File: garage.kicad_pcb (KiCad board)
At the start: 2 copper layers, 90 x 100 mm, 32 parts, among them J1 AC L/N, J2 Gate, K1 Relay_SPST-NO, K2 Relay_SPST-NO, Q1 2N5551, Q2 2N5551, SW1 Button, SW2 Radio, U1 LM2940T-5.0/NOPB, U2 ACS712xLCTR-05B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

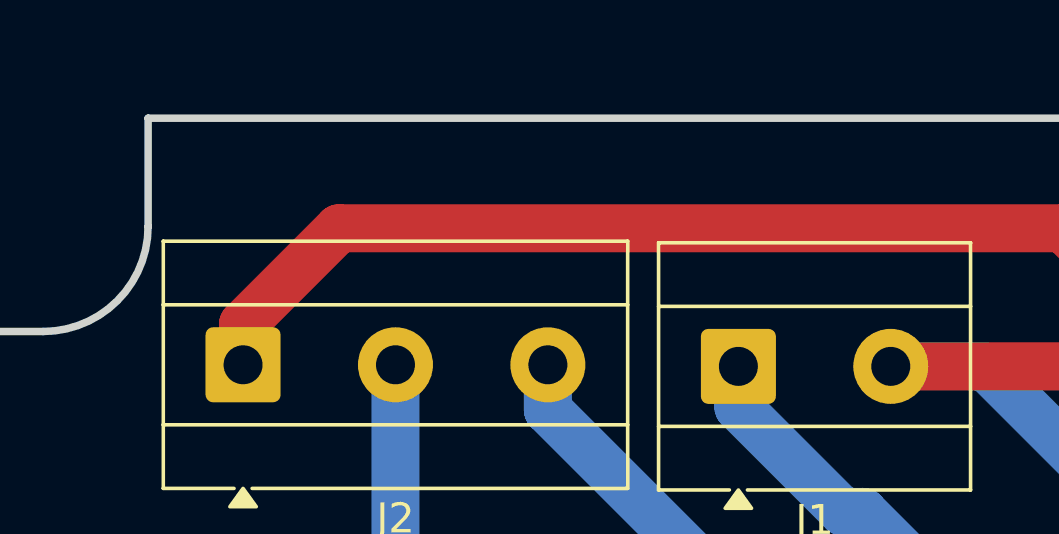
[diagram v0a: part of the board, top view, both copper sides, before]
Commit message: Reorganize and make suitable for publication.
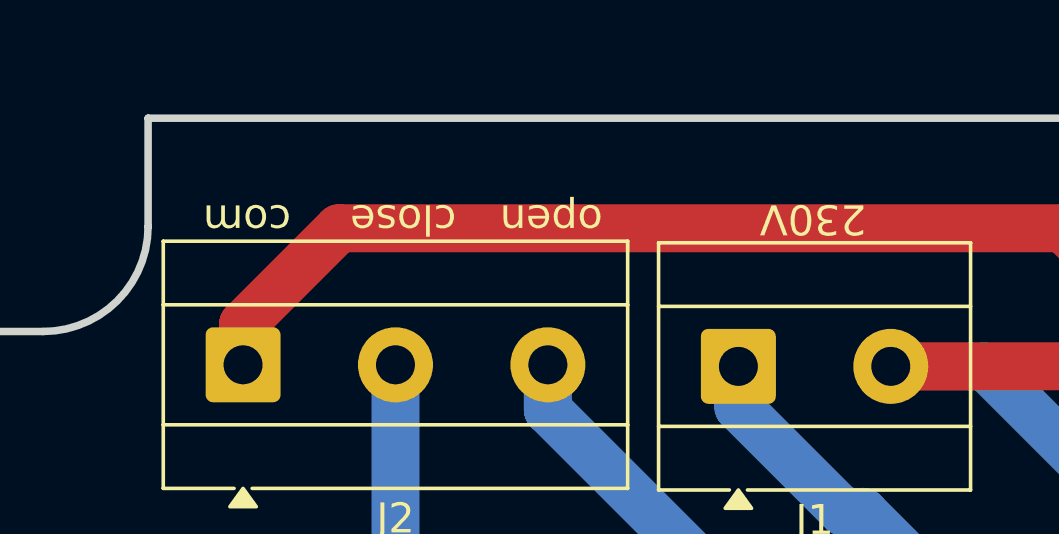
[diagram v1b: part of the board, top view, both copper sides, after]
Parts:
- RV1: value R_Potentiometer -> 10k
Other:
- board text added: "https://github.com/macdems/Garage"
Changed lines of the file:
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@@
 		(property ki_fp_filters "R_*")
 		(sheetname "/")
-		(sheetfile "Garaż.kicad_sch")
+		(sheetfile "garage.kicad_sch")
 		(attr through_hole)
 		(fp_line
@@
 		(property ki_fp_filters "SOIC*3.9x4.9mm*P1.27mm* DIP*W7.62mm* TO*99* OnSemi*Micro8* TSSOP*3x3mm*P0.65mm* TSSOP*4.4x3mm*P0.65mm* MSOP*3x3mm*P0.65mm* SSOP*3.9x4.9mm*P0.635mm* LFCSP*2x2mm*P0.5mm* *SIP* SOIC*5.3x6.2mm*P1.27mm*")
 		(sheetname "/")
-		(sheetfile "Garaż.kicad_sch")
+		(sheetfile "garage.kicad_sch")
 		(attr through_hole)
 		(fp_line
@@
 		(property ki_fp_filters "Connector*:*_1x??_*")
 		(sheetname "/")
-		(sheetfile "Garaż.kicad_sch")
+		(sheetfile "garage.kicad_sch")
 		(attr through_hole)
 		(fp_line
@@
 			(layer "F.Fab")
 		)
+		(fp_text user "close"
+			(at 7.106191 -5.4356 180)
+			(unlocked yes)
+			(layer "F.SilkS")
+			(effects
+				(font
+					(size 1 1)
+					(thickness 0.1)
+				)
+				(justify left bottom)
+			)
+		)
+		(fp_text user "open"
+			(at 11.9888 -5.4356 180)
+			(unlocked yes)
+			(layer "F.SilkS")
+			(effects
+				(font
+					(size 1 1)
+					(thickness 0.1)
+				)
+				(justify left bottom)
+			)
+		)
+		(fp_text user "com"
+			(at 1.597619 -5.4356 180)
+			(unlocked yes)
+			(layer "F.SilkS")
+			(effects
+				(font
+					(size 1 1)
+					(thickness 0.1)
+				)
+				(justify left bottom)
+			)
+		)
 		(fp_text user "${REFERENCE}"
 			(at 5.08 3 0)
@@
 		(property ki_fp_filters "R_*")
 		(sheetname "/")
-		(sheetfile "Garaż.kicad_sch")
+		(sheetfile "garage.kicad_sch")
 		(attr through_hole)
 		(fp_line
@@
 		(property ki_fp_filters "MountingHole*")
 		(sheetname "/")
-		(sheetfile "Garaż.kicad_sch")
+		(sheetfile "garage.kicad_sch")
 		(attr exclude_from_pos_files exclude_from_bom)
 		(fp_circle
@@
 		(property ki_fp_filters "CP_*")
 		(sheetname "/")
-		(sheetfile "Garaż.kicad_sch")
+		(sheetfile "garage.kicad_sch")
 		(attr through_hole)
 		(fp_line
@@
 		(property ki_fp_filters "C_*")
 		(sheetname "/")
-		(sheetfile "Garaż.kicad_sch")
+		(sheetfile "garage.kicad_sch")
 		(attr through_hole)
 		(fp_line
@@
 		)
 		(sheetname "/")
-		(sheetfile "Garaż.kicad_sch")
+		(sheetfile "garage.kicad_sch")
 		(attr through_hole)
 		(fp_line
@@
 		(property ki_fp_filters "NDE3")
 		(sheetname "/")
-		(sheetfile "Garaż.kicad_sch")
+		(sheetfile "garage.kicad_sch")
 		(attr through_hole)
 		(fp_line
@@
 		(property ki_fp_filters "SOIC*3.9x4.9m*P1.27mm*")
 		(sheetname "/")
-		(sheetfile "Garaż.kicad_sch")
+		(sheetfile "garage.kicad_sch")
 		(attr smd)
 		(fp_line
@@
 		(property ki_fp_filters "Connector*:*_1x??_*")
 		(sheetname "/")
-		(sheetfile "Garaż.kicad_sch")
+		(sheetfile "garage.kicad_sch")
 		(attr through_hole)
 		(fp_line
@@
 			(layer "F.Fab")
 		)
+		(fp_text user "230V"
+			(at 2.4892 -5.4881 180)
+			(unlocked yes)
+			(layer "F.SilkS")
+			(effects
+				(font
+					(size 1 1)
+					(thickness 0.1)
+				)
+				(justify bottom)
+			)
+		)
 		(fp_text user "${REFERENCE}"
 			(at 2.54 3 0)
@@
 		(property ki_fp_filters "R_*")
 		(sheetname "/")
-		(sheetfile "Garaż.kicad_sch")
+		(sheetfile "garage.kicad_sch")
 		(attr through_hole)
 		(fp_line
@@
 		(property ki_fp_filters "TO-???* *_Diode_* *SingleDiode* D_*")
 		(sheetname "/")
-		(sheetfile "Garaż.kicad_sch")
+		(sheetfile "garage.kicad_sch")
 		(attr through_hole)
 		(fp_line
@@
 		)
 		(sheetname "/")
-		(sheetfile "Garaż.kicad_sch")
+		(sheetfile "garage.kicad_sch")
 		(attr through_hole)
 		(fp_line
@@
 		(property ki_fp_filters "Relay?SPST*")
 		(sheetname "/")
-		(sheetfile "Garaż.kicad_sch")
+		(sheetfile "garage.kicad_sch")
 		(attr through_hole)
 		(fp_line
@@
 		)
 		(sheetname "/")
-		(sheetfile "Garaż.kicad_sch")
+		(sheetfile "garage.kicad_sch")
 		(attr through_hole)
 		(fp_line
@@
 		)
 		(sheetname "/")
-		(sheetfile "Garaż.kicad_sch")
+		(sheetfile "garage.kicad_sch")
 		(attr through_hole)
 		(fp_line
@@
 			)
 		)
-		(property "Value" "R_Potentiometer"
+		(property "Value" "10k"
 			(at 2.6 7.4 0)
 			(layer "F.Fab")
@@
 		(property ki_fp_filters "Potentiometer*")
 		(sheetname "/")
-		(sheetfile "Garaż.kicad_sch")
+		(sheetfile "garage.kicad_sch")
 		(attr through_hole)
 		(fp_line
@@
 		(property ki_fp_filters "MountingHole*")
 		(sheetname "/")
-		(sheetfile "Garaż.kicad_sch")
+		(sheetfile "garage.kicad_sch")
 		(attr exclude_from_pos_files exclude_from_bom)
 		(fp_circle
@@
 		(property ki_fp_filters "CP_*")
 		(sheetname "/")
-		(sheetfile "Garaż.kicad_sch")
+		(sheetfile "garage.kicad_sch")
 		(attr through_hole)
 		(fp_line
@@
 		(property ki_fp_filters "R_*")
 		(sheetname "/")
-		(sheetfile "Garaż.kicad_sch")
+		(sheetfile "garage.kicad_sch")
 		(attr through_hole)
 		(fp_line
@@
 		(property ki_fp_filters "R_*")
 		(sheetname "/")
-		(sheetfile "Garaż.kicad_sch")
+		(sheetfile "garage.kicad_sch")
 		(attr through_hole)
 		(fp_line
@@
 		(property ki_fp_filters "R_*")
 		(sheetname "/")
-		(sheetfile "Garaż.kicad_sch")
+		(sheetfile "garage.kicad_sch")
 		(attr through_hole)
 		(fp_line
@@
 		(property ki_fp_filters "MountingHole*")
 		(sheetname "/")
-		(sheetfile "Garaż.kicad_sch")
+		(sheetfile "garage.kicad_sch")
 		(attr exclude_from_pos_files exclude_from_bom)
 		(fp_circle
@@
 		(property ki_fp_filters "Converter*ACDC*Hi?Link*HLK?30M*")
 		(sheetname "/")
-		(sheetfile "Garaż.kicad_sch")
+		(sheetfile "garage.kicad_sch")
 		(attr through_hole)
 		(fp_line
@@
 		(property ki_fp_filters "R_*")
 		(sheetname "/")
-		(sheetfile "Garaż.kicad_sch")
+		(sheetfile "garage.kicad_sch")
 		(attr through_hole)
 		(fp_line
@@
 		(property ki_fp_filters "Heatsink_*")
 		(sheetname "/")
-		(sheetfile "Garaż.kicad_sch")
+		(sheetfile "garage.kicad_sch")
 		(attr through_hole)
 		(fp_line
@@
 		(property ki_fp_filters "TO-???* *_Diode_* *SingleDiode* D_*")
 		(sheetname "/")
-		(sheetfile "Garaż.kicad_sch")
+		(sheetfile "garage.kicad_sch")
 		(attr through_hole)
 		(fp_line
@@
 		)
 		(sheetname "/")
-		(sheetfile "Garaż.kicad_sch")
+		(sheetfile "garage.kicad_sch")
 		(attr through_hole)
 		(fp_line
@@
 		(property ki_fp_filters "C_*")
 		(sheetname "/")
-		(sheetfile "Garaż.kicad_sch")
+		(sheetfile "garage.kicad_sch")
 		(attr through_hole)
 		(fp_line
@@
 		(property ki_fp_filters "R_*")
 		(sheetname "/")
-		(sheetfile "Garaż.kicad_sch")
+		(sheetfile "garage.kicad_sch")
 		(attr through_hole)
 		(fp_line
@@
 		(property ki_fp_filters "Relay?SPST*")
 		(sheetname "/")
-		(sheetfile "Garaż.kicad_sch")
+		(sheetfile "garage.kicad_sch")
 		(attr through_hole)
 		(fp_line
@@
 		(layer "Edge.Cuts")
 	)
+	(gr_text "https://github.com/macdems/Garage"
+		(at 113.665 116.84 0)
+		(layer "B.SilkS")
+		(effects
+			(font
+				(size 2 2)
+				(thickness 0.25)
+			)
+			(justify bottom mirror)
+		)
+	)
 	(segment

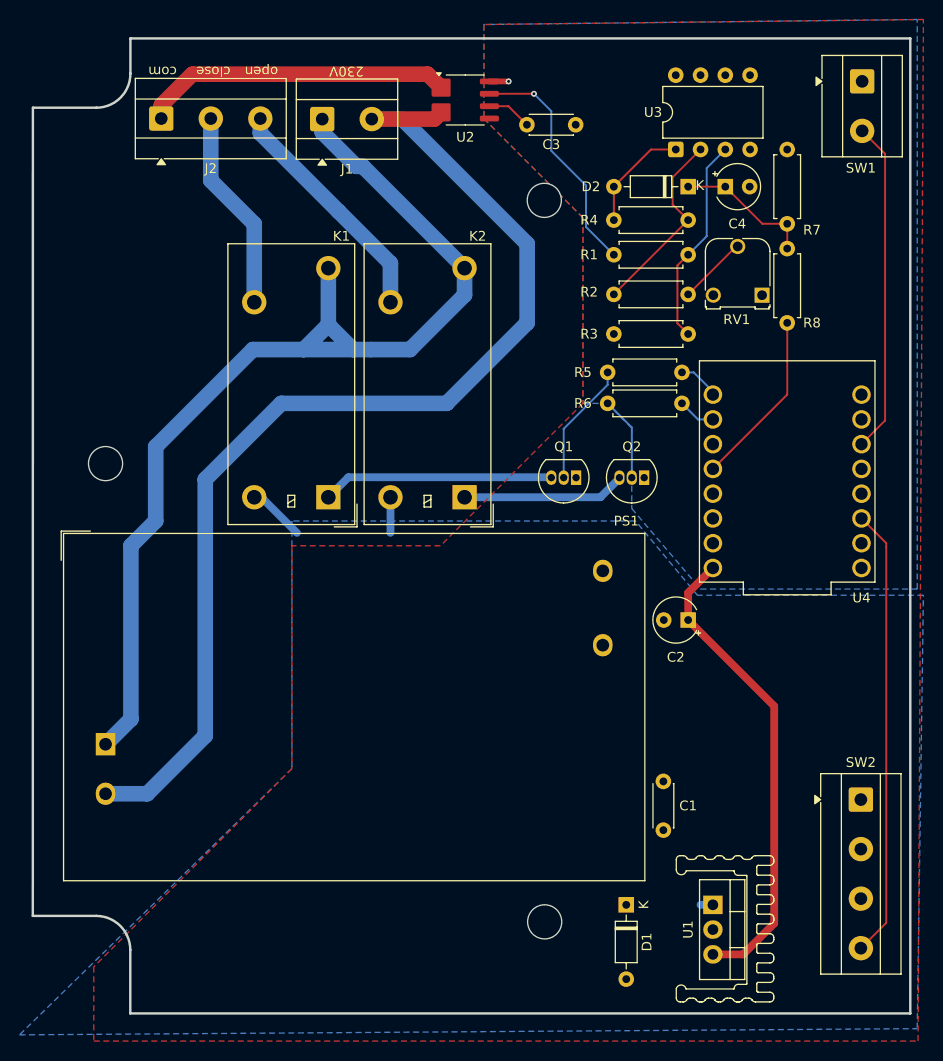
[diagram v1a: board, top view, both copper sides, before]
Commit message: Design rules fix
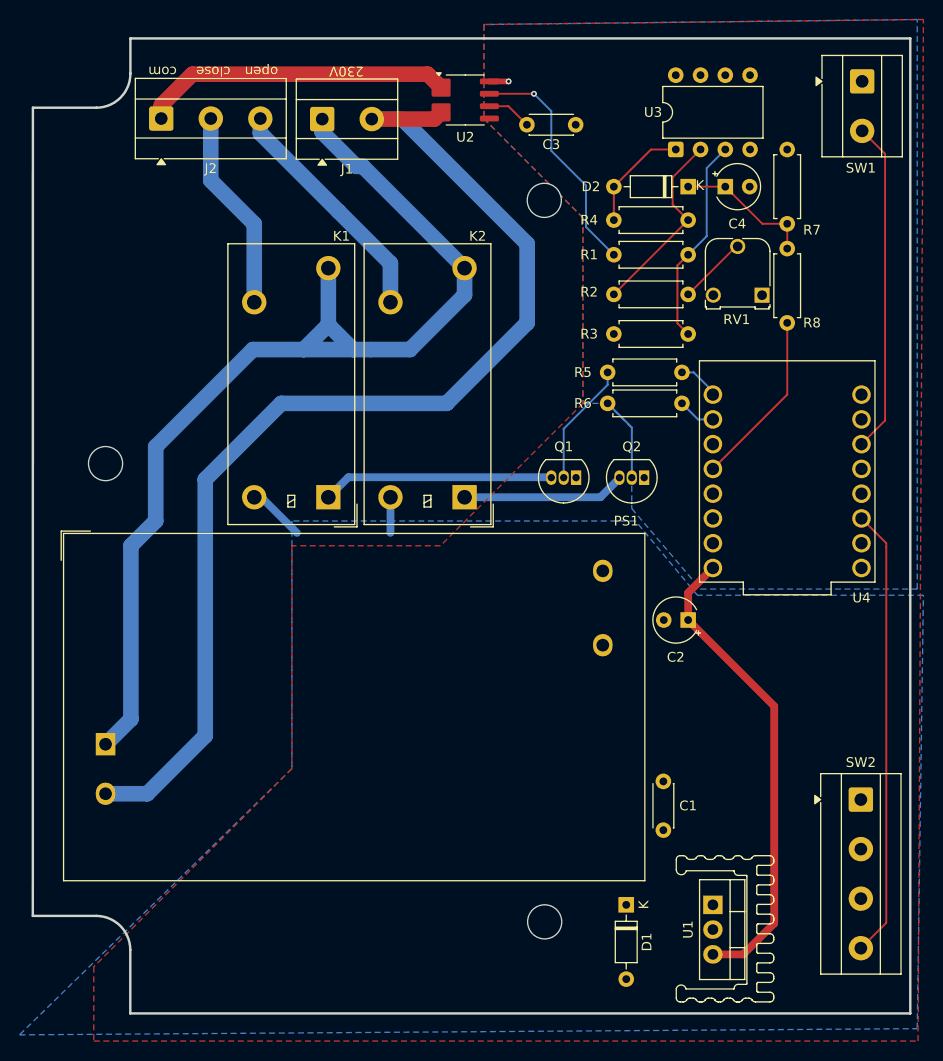
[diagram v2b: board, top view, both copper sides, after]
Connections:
- J2 pad 1: AC/N -> /AC/NI
- U2 pad 1: AC/N -> /AC/NI
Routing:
- net /AC/NI: track 0.00 -> 32.0 mm
- net AC/N: track 147.3 -> 115.4 mm
- net +12V: track 10.8 -> 9.54 mm
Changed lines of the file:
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@@
 	(net 31 "unconnected-(U4-GPIO2-Pad2)")
 	(net 32 "unconnected-(U4-GPIO4-Pad4)")
+	(net 33 "/AC{slash}NI")
 	(footprint "Resistor_THT:R_Axial_DIN0207_L6.3mm_D2.5mm_P7.62mm_Horizontal"
 		(layer "F.Cu")
@@
 			)
 		)
-		(property "Datasheet" ""
+		(property "Datasheet" "~"
 			(at 0 0 0)
 			(unlocked yes)
@@
 			)
 		)
-		(property "Datasheet" ""
+		(property "Datasheet" "~"
 			(at 0 0 0)
 			(layer "F.Fab")
@@
 			(remove_unused_layers no)
 			(roundrect_rratio 0.1)
-			(net 7 "AC{slash}N")
+			(net 33 "/AC{slash}NI")
 			(pinfunction "Pin_1")
 			(pintype "passive")
@@
 			)
 		)
-		(property "Datasheet" ""
+		(property "Datasheet" "~"
 			(at 0 0 0)
 			(unlocked yes)
@@
 			)
 		)
-		(property "Datasheet" ""
+		(property "Datasheet" "~"
 			(at 0 0 0)
 			(unlocked yes)
@@
 			)
 		)
-		(property "Datasheet" ""
+		(property "Datasheet" "~"
 			(at 0 0 0)
 			(layer "F.Fab")
@@
 			)
 		)
-		(property "Datasheet" ""
+		(property "Datasheet" "~"
 			(at 0 0 0)
 			(layer "F.Fab")
@@
 			)
 		)
-		(property "Datasheet" ""
+		(property "Datasheet" "~"
 			(at 0 0 270)
 			(layer "F.Fab")
@@
 			(layers "F.Cu" "F.Mask" "F.Paste")
 			(roundrect_rratio 0.08021390374)
-			(net 7 "AC{slash}N")
+			(net 33 "/AC{slash}NI")
 			(pinfunction "IP+")
 			(pintype "passive")
@@
 			)
 		)
-		(property "Datasheet" ""
+		(property "Datasheet" "~"
 			(at 0 0 0)
 			(layer "F.Fab")
@@
 			)
 		)
-		(property "Datasheet" ""
+		(property "Datasheet" "~"
 			(at 0 0 0)
 			(unlocked yes)
@@
 			)
 		)
-		(property "Datasheet" ""
+		(property "Datasheet" "~"
 			(at 0 0 270)
 			(unlocked yes)
@@
 			)
 		)
-		(property "Datasheet" ""
+		(property "Datasheet" "~"
 			(at 0 0 90)
 			(unlocked yes)
@@
 			)
 		)
-		(property "Datasheet" ""
+		(property "Datasheet" "~"
 			(at 0 0 180)
 			(unlocked yes)
@@
 			)
 		)
-		(property "Datasheet" ""
+		(property "Datasheet" "~"
 			(at 0 0 0)
 			(unlocked yes)
@@
 			)
 		)
-		(property "Datasheet" ""
+		(property "Datasheet" "~"
 			(at 0 0 0)
 			(layer "F.Fab")
@@
 			)
 		)
-		(property "Datasheet" ""
+		(property "Datasheet" "~"
 			(at 0 0 0)
 			(unlocked yes)
@@
 			)
 		)
-		(property "Datasheet" ""
+		(property "Datasheet" "~"
 			(at 0 0 90)
 			(unlocked yes)
@@
 			)
 		)
-		(property "Datasheet" ""
+		(property "Datasheet" "~"
 			(at 0 0 0)
 			(unlocked yes)
@@
 			)
 		)
-		(property "Datasheet" ""
+		(property "Datasheet" "~"
 			(at 0 0 0)
 			(unlocked yes)
@@
 			)
 		)
-		(property "Datasheet" ""
+		(property "Datasheet" "~"
 			(at 0 0 90)
 			(unlocked yes)
@@
 			)
 		)
-		(property "Datasheet" ""
+		(property "Datasheet" "~"
 			(at 0 0 270)
 			(unlocked yes)
@@
 			)
 		)
-		(property "Datasheet" ""
+		(property "Datasheet" "~"
 			(at 0 0 180)
 			(unlocked yes)
@@
 			)
 		)
-		(property "Datasheet" ""
+		(property "Datasheet" "~"
 			(at 0 0 270)
 			(layer "F.Fab")
@@
 			)
 		)
-		(property "Datasheet" ""
+		(property "Datasheet" "~"
 			(at 0 0 90)
 			(layer "F.Fab")
@@
 			)
 		)
-		(property "Datasheet" ""
+		(property "Datasheet" "~"
 			(at 0 0 0)
 			(unlocked yes)
@@
 			)
 		)
-		(property "Datasheet" ""
+		(property "Datasheet" "~"
 			(at 0 0 90)
 			(unlocked yes)
@@
 	)
 	(segment
-		(start 125.795 135.255)
-		(end 124.525 135.255)
-		(width 0.8)
-		(layer "B.Cu")
-		(net 2)
-	)
-	(segment
 		(start 92.7225 97.1025)
 		(end 92.7225 93.4525)
@@
 	)
 	(segment
-		(start 97.92 51.435)
-		(end 96.544 50.059)
-		(width 1.6)
-		(layer "F.Cu")
-		(net 7)
-	)
-	(segment
-		(start 96.544 50.059)
-		(end 72.409914 50.059)
-		(width 1.6)
-		(layer "F.Cu")
-		(net 7)
-	)
-	(segment
 		(start 90.805 54.6625)
 		(end 97.2325 54.6625)
@@
 	)
 	(segment
-		(start 69.215 53.253914)
-		(end 69.215 54.61)
-		(width 1.6)
-		(layer "F.Cu")
-		(net 7)
-	)
-	(segment
-		(start 72.409914 50.059)
-		(end 69.215 53.253914)
-		(width 1.6)
-		(layer "F.Cu")
-		(net 7)
-	)
-	(segment
 		(start 106.745 67.459825)
 		(end 106.745 75.565)
@@
 		(net 29)
 	)
+	(segment
+		(start 97.92 51.435)
+		(end 96.544 50.059)
+		(width 1.6)
+		(layer "F.Cu")
+		(net 33)
+	)
+	(segment
+		(start 69.215 53.253914)
+		(end 69.215 54.61)
+		(width 1.6)
+		(layer "F.Cu")
+		(net 33)
+	)
+	(segment
+		(start 72.409914 50.059)
+		(end 96.544 50.059)
+		(width 1.6)
+		(layer "F.Cu")
+		(net 33)
+	)
+	(segment
+		(start 72.409914 50.059)
+		(end 69.215 53.253914)
+		(width 1.6)
+		(layer "F.Cu")
+		(net 33)
+	)
 	(zone
